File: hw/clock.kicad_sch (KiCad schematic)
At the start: 39 parts, among them J1 USB4105-GF-A, SW1 SW_Push, SW2 SW_Push, U1 LPC812M101JDH20, U10 HDSP-5321 Common Anode, U11 HDSP-5321 Common Anode, U12 HDSP-5321 Common Anode, U13 MCP9808T-E/MS, U2 INTERFACE-FT230XS-R_SSOP16_, U3 SN74HC595DR, U4 SN74HC595DR, U5 SN74HC595DR, U6 SN74HC595DR, U7 SN74HC595DR, U8 SN74HC595DR, U9 MCP7940MT-I_SN, Y1 30MHz, Y2 32.768KHz

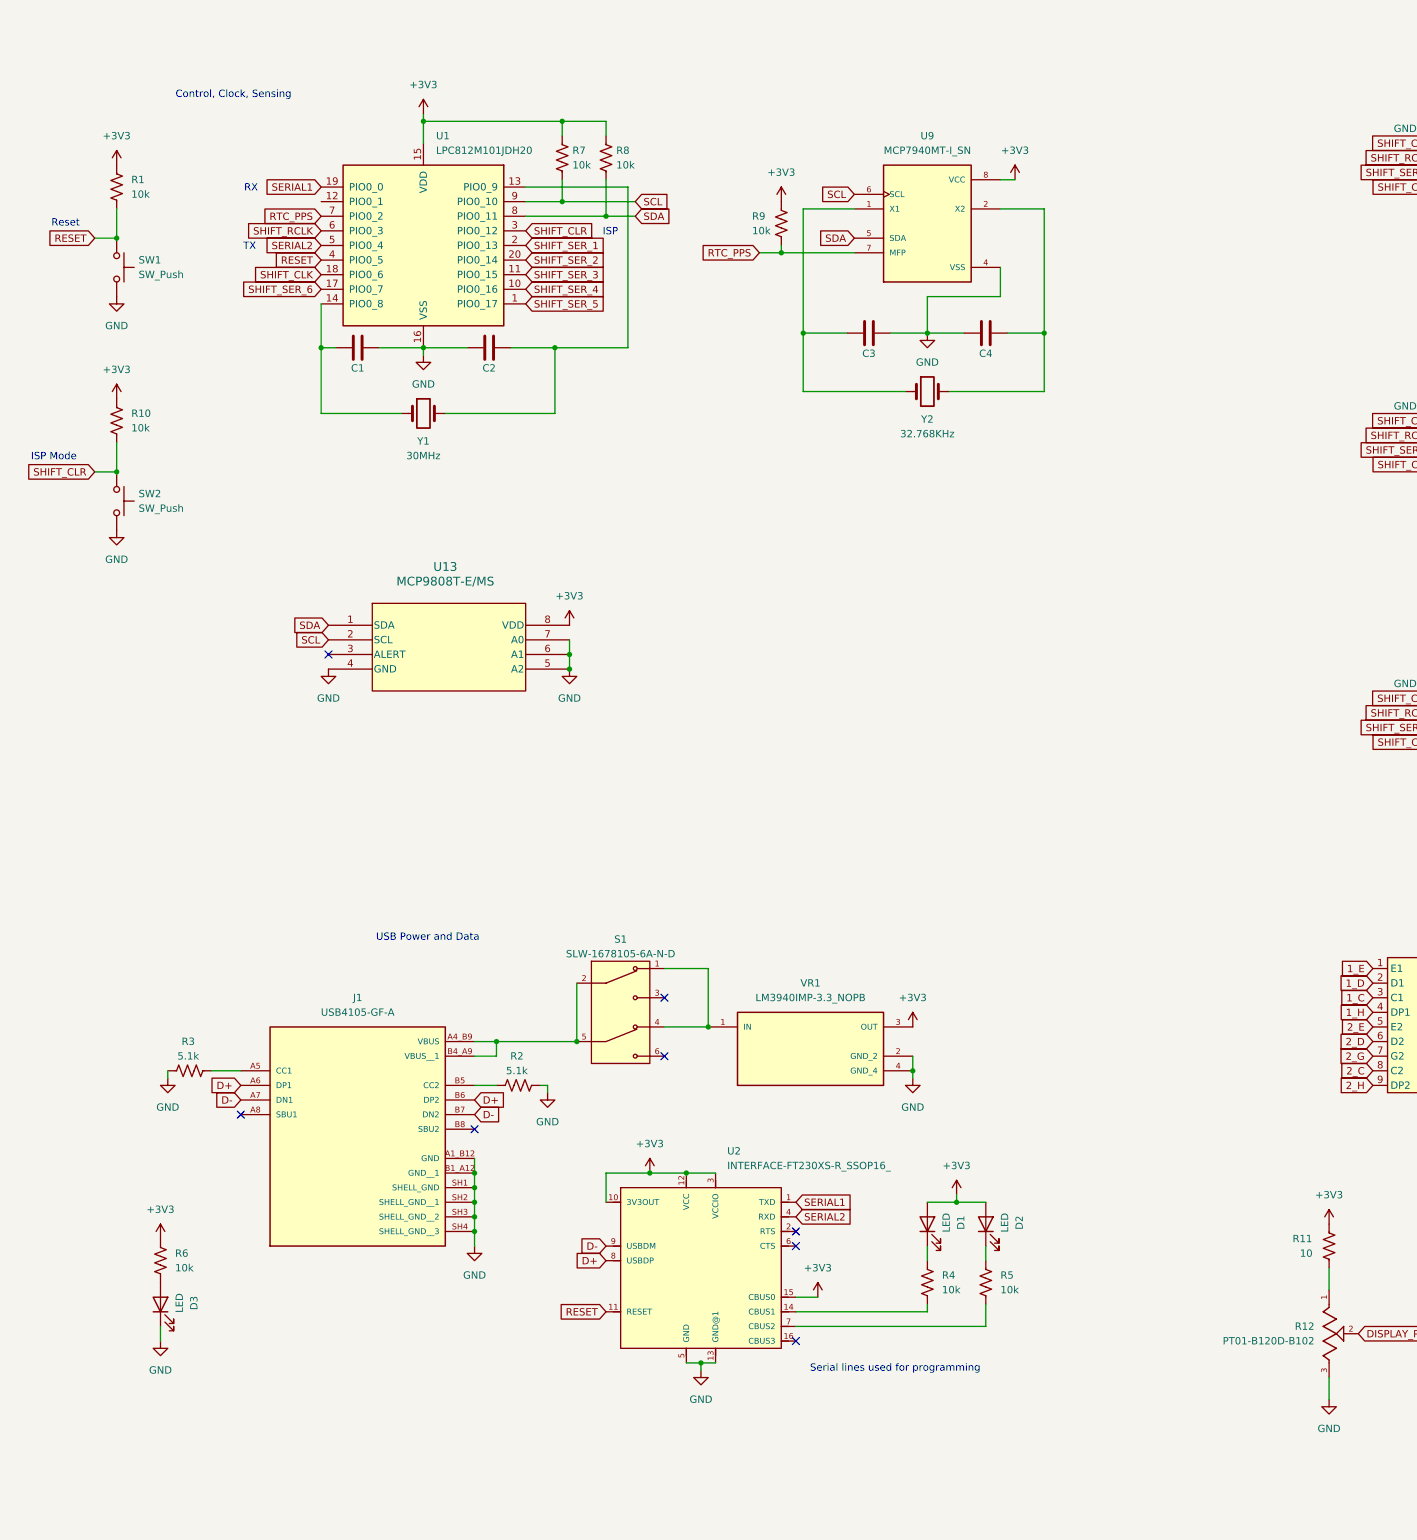
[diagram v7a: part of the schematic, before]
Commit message: USB output
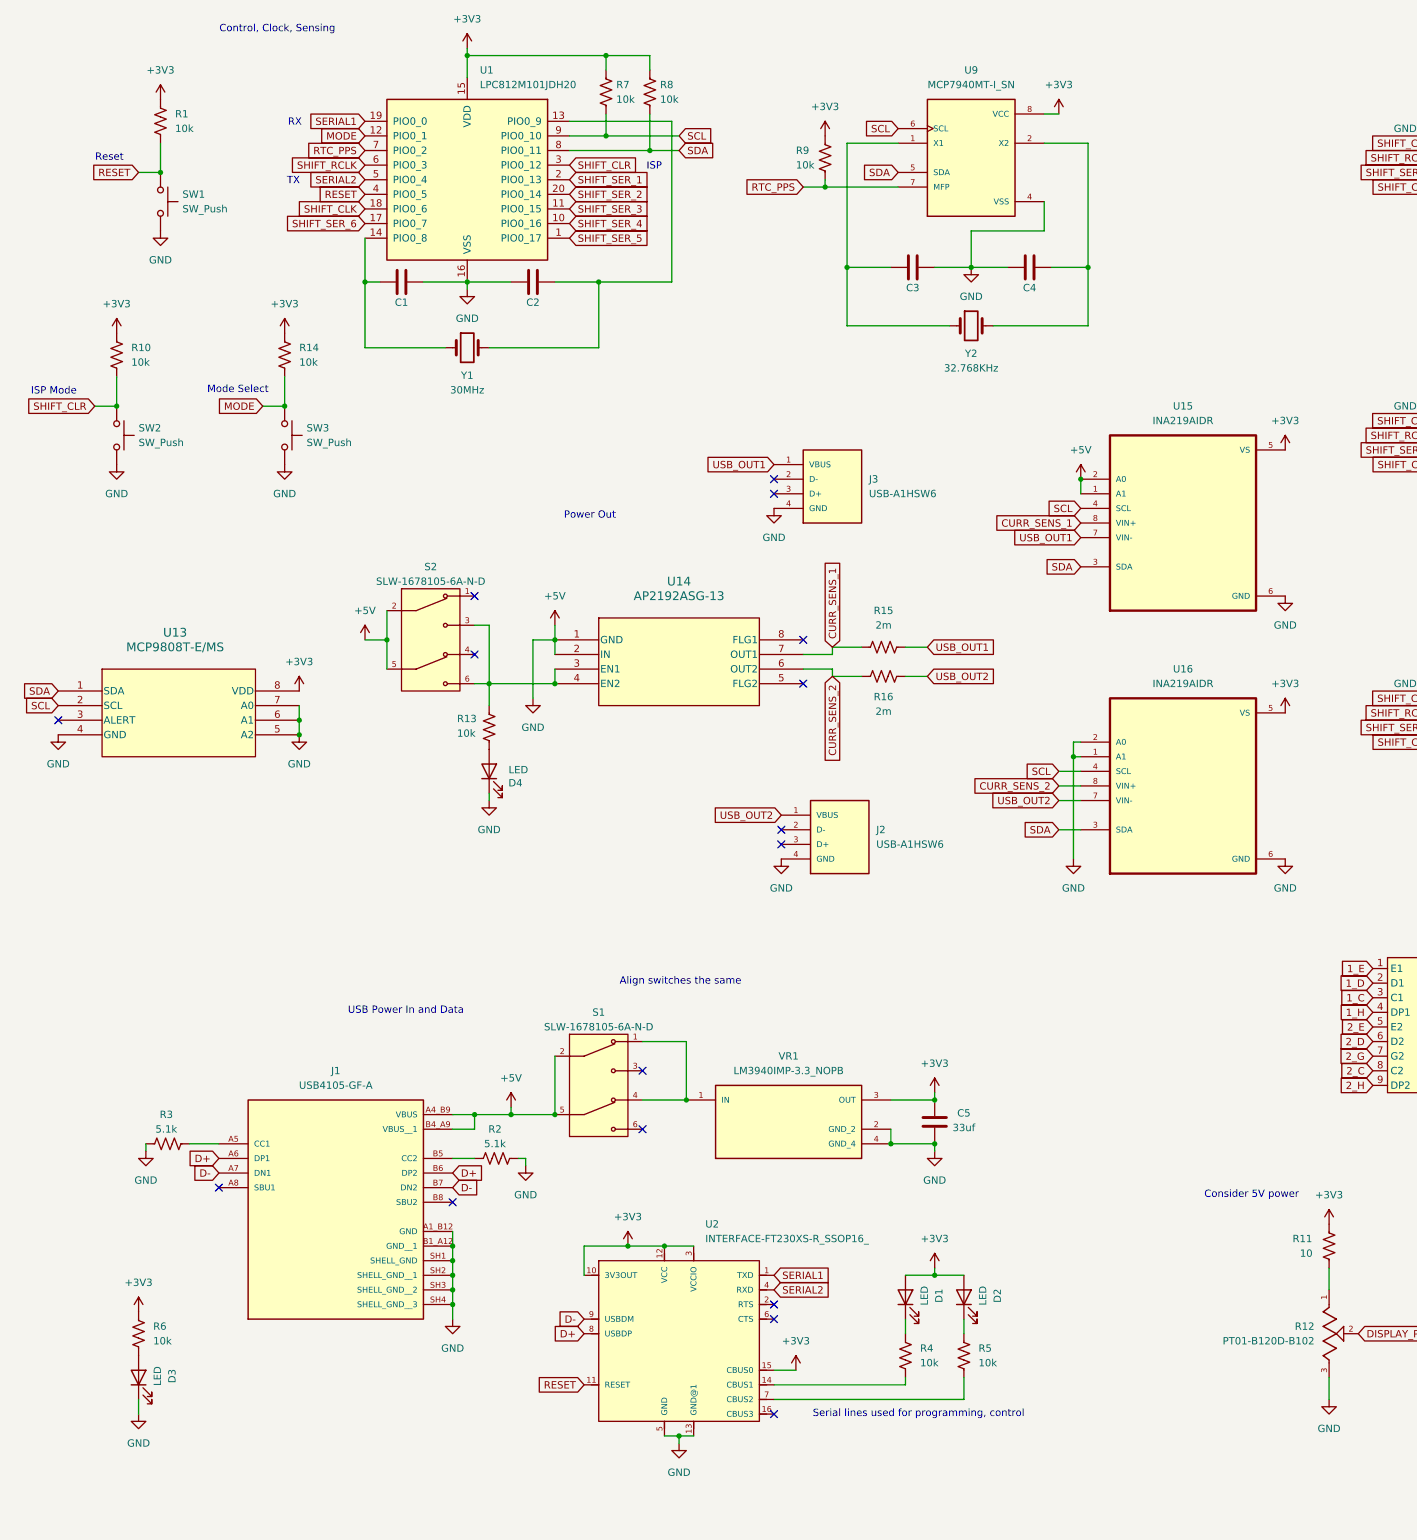
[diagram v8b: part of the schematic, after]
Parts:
- added C5: 33uf, Capacitor_SMD:C_0805_2012Metric, symbol Device:C
- added D4: LED, LED_SMD:LED_0805_2012Metric, symbol Device:LED
- added J2, J3: USB-A1HSW6, Clock:OST_USB-A1HSW6, symbol USB-A1HSW6:USB-A1HSW6
- added R13, R14: 10k, Resistor_SMD:R_0805_2012Metric, symbol Device:R_US
- added R15, R16: 2m, Resistor_SMD:R_0805_2012Metric, symbol Device:R_US
- added S2: SLW-1678105-6A-N-D, Clock:SW_SLW-1678105-6A-N-D, symbol SLW-1678105-6A-N-D:SLW-1678105-6A-N-D
- added SW3: SW_Push, symbol Switch:SW_Push
- added U14: AP2192ASG-13, Clock:AP2192ASG_13, symbol AP2192ASG_13:AP2192ASG-13
- added U15, U16: INA219AIDR, Clock:INA219AIDR, symbol INA219AIDR:INA219AIDR
- C1, C2, C3, C4: footprint (none) -> Capacitor_SMD:C_0805_2012Metric
- R12: footprint PT01-B120D-B102:TRIM_PT01-B120D-B102 -> Clock:TRIM_PT01-B120D-B102
- U13: footprint MSOP8_MC_MCH -> Clock:MCP9808T
- U3, U4, U5, U6, U7, U8: footprint SN74HC595DR:SOIC127P600X175-16N -> Clock:SOIC127P600X175-16N
- U9: footprint MCP7940MT-I_SN:SOIC127P600X175-8N -> Clock:SOIC127P600X175-8N
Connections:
- net GND is gone; now on net +5V: C1.2, C2.1, C3.2, C4.1, D3.1 (K), J1.A1_B12 (GND), J1.B1_A12 (GND__1), J1.SH1 (SHELL_GND), J1.SH2 (SHELL_GND__1), J1.SH3 (SHELL_GND__2), J1.SH4 (SHELL_GND__3), R12.3, R2.1, R3.2, SW1.2, SW2.2, U1.16 (VSS), U13.4 (GND), U13.5 (A2), U13.6 (A1), U13.7 (A0), U2.13 (GND@1), U2.5 (GND), U3.13 (~{OE}), U3.8 (GND), U4.13 (~{OE}), U4.8 (GND), U5.13 (~{OE}), U5.8 (GND), U6.13 (~{OE}), U6.8 (GND), U7.13 (~{OE}), U7.8 (GND), U8.13 (~{OE}), U8.8 (GND), U9.4 (VSS), VR1.2 (GND_2), VR1.4 (GND_4)
- net +3V3: now also C5.2, R14.2, U15.5 (VS), U16.5 (VS)
- net SCL: now also U15.4 (SCL), U16.4 (SCL)
- net SDA: now also U15.3 (SDA), U16.3 (SDA)
- net +5V: now reaches J1.A4_B9 (VBUS), J1.B4_A9 (VBUS__1), S1.2, S1.5
- net +5V: now also C5.1, D4.1 (K), J2.4 (GND), J3.4 (GND), S2.2, S2.5, SW3.2, U14.1 (GND), U14.2 (IN), U15.1 (A1), U15.2 (A0), U15.6 (GND), U16.1 (A1), U16.2 (A0), U16.6 (GND)
- net MODE: now reaches U1.12 (PIO0_1)
- net MODE: now also R14.1, SW3.1
- new net: R13.2, S2.3, S2.6, U14.3 (EN1), U14.4 (EN2)
- new net: D4.2 (A), R13.1
- new net CURR_SENS_1: R15.2, U14.7 (OUT1), U15.8 (VIN+)
- new net CURR_SENS_2: R16.2, U14.6 (OUT2), U16.8 (VIN+)
- new net USB_OUT1: J3.1 (VBUS), R15.1, U15.7 (VIN-)
- new net USB_OUT2: J2.1 (VBUS), R16.1, U16.7 (VIN-)
- no-connect marks 14 -> 22
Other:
- note added: "Align switches the same"
- note added: "Consider 5V power"
- note added: "Mode Select"
- note added: "Power Out"
- note added: "Serial lines used for programming, control"
- note added: "USB Power In and Data"
- note removed: "Serial lines used for programming"
- note removed: "USB Power and Data"
- moved on the sheet: C1, C2, C3, C4, D1, D2, D3, J1, R1, R10, R2, R3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
